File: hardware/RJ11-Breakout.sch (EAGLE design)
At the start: 8 parts

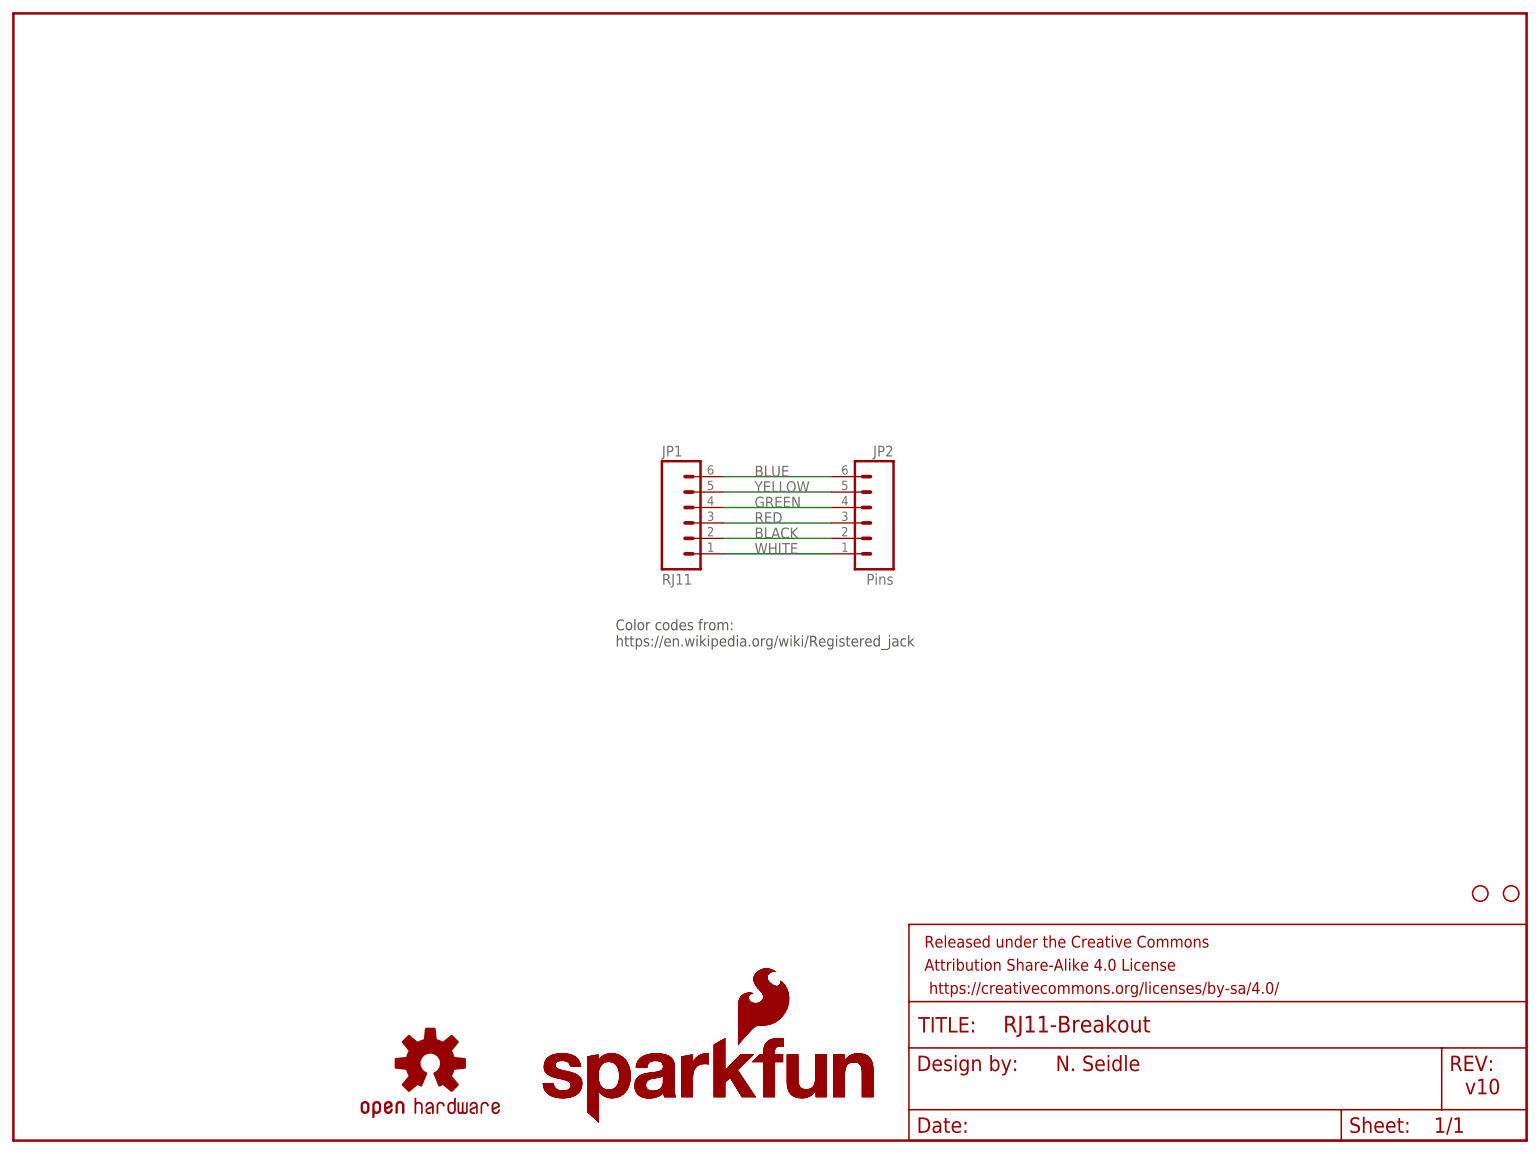
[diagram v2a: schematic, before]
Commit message: Creating panel of two
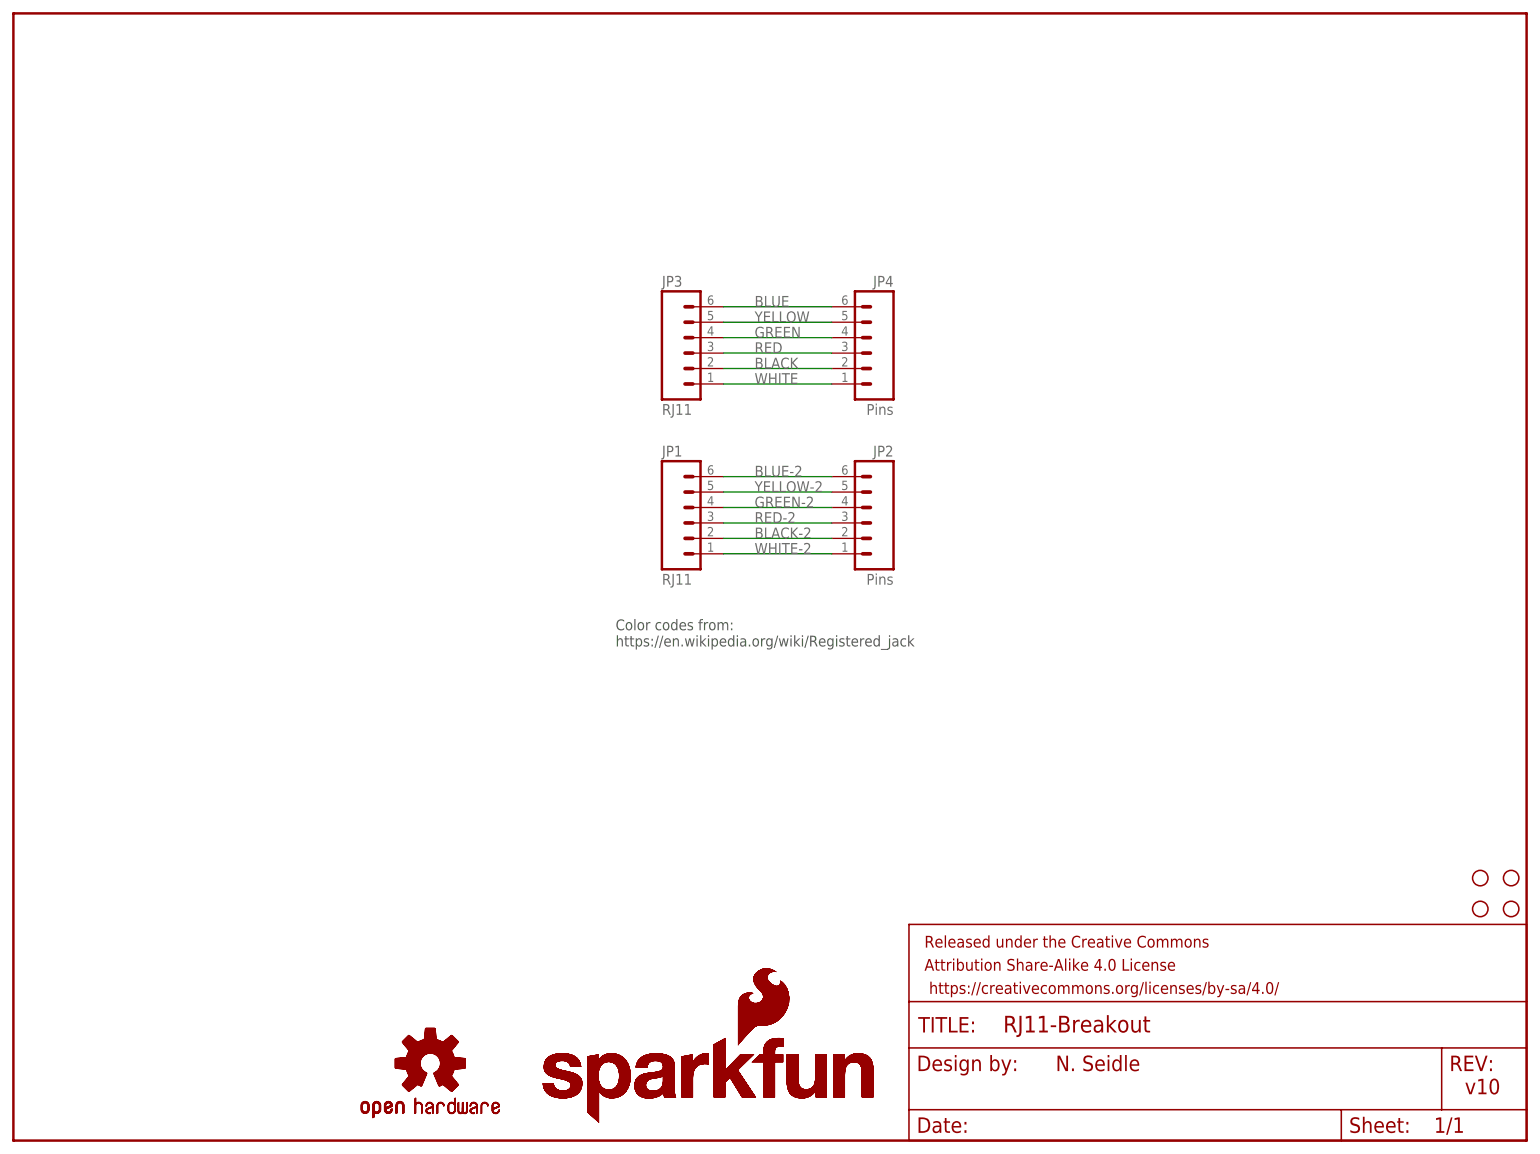
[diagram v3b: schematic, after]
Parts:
- added H2, H4: STAND-OFF, SparkFun-Electromechanical:STAND-OFF
- added JP3: RJ11, SparkFun-Connectors:RJ11-6PTH
- added JP4: Pins, SparkFun-Connectors:M06SILK_FEMALE_PTH
- added LOGO4, LOGO5: SFE_LOGO_NAME_FLAME.1_INCH, SparkFun-Aesthetics:SFE_LOGO_NAME_FLAME.1_INCH
- added LOGO6: OSHW-LOGOMINI, SparkFun-Aesthetics:OSHW-LOGOMINI
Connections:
- new net BLACK-2: JP1.2, JP2.2
- new net BLUE-2: JP1.6, JP2.6
- new net GREEN-2: JP1.4, JP2.4
- new net RED-2: JP1.3, JP2.3
- new net WHITE-2: JP1.1, JP2.1
- new net YELLOW-2: JP1.5, JP2.5
- net BLACK: now also JP3.2, JP4.2; no longer JP1.2, JP2.2
- net BLUE: now also JP3.6, JP4.6; no longer JP1.6, JP2.6
- net GREEN: now also JP3.4, JP4.4; no longer JP1.4, JP2.4
- net RED: now also JP3.3, JP4.3; no longer JP1.3, JP2.3
- net WHITE: now also JP3.1, JP4.1; no longer JP1.1, JP2.1
- net YELLOW: now also JP3.5, JP4.5; no longer JP1.5, JP2.5
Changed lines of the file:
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@@
 <part name="H1" library="SparkFun-Electromechanical" deviceset="STAND-OFF" device=""/>
 <part name="H3" library="SparkFun-Electromechanical" deviceset="STAND-OFF" device=""/>
+<part name="JP3" library="SparkFun-Connectors" deviceset="RJ11-6" device="PTH" value="RJ11"/>
+<part name="JP4" library="SparkFun-Connectors" deviceset="M06" device="SILK_FEMALE_PTH" value="Pins"/>
+<part name="H2" library="SparkFun-Electromechanical" deviceset="STAND-OFF" device=""/>
+<part name="H4" library="SparkFun-Electromechanical" deviceset="STAND-OFF" device=""/>
+<part name="LOGO4" library="SparkFun-Aesthetics" deviceset="SFE_LOGO_NAME_FLAME" device=".1_INCH"/>
+<part name="LOGO5" library="SparkFun-Aesthetics" deviceset="SFE_LOGO_NAME_FLAME" device=".1_INCH"/>
+<part name="LOGO6" library="SparkFun-Aesthetics" deviceset="OSHW-LOGO" device="MINI"/>
 </parts>
 <sheets>
@@
 <instance part="LOGO2" gate="G$1" x="86.36" y="2.54"/>
 <instance part="LOGO3" gate="G$1" x="68.58" y="12.7"/>
-<instance part="H1" gate="G$1" x="246.38" y="40.64"/>
-<instance part="H3" gate="G$1" x="241.3" y="40.64"/>
+<instance part="H1" gate="G$1" x="246.38" y="43.18"/>
+<instance part="H3" gate="G$1" x="241.3" y="43.18"/>
+<instance part="JP3" gate="G$1" x="111.76" y="129.54"/>
+<instance part="JP4" gate="G$1" x="139.7" y="129.54" rot="MR0"/>
+<instance part="H2" gate="G$1" x="241.3" y="38.1"/>
+<instance part="H4" gate="G$1" x="246.38" y="38.1"/>
+<instance part="LOGO4" gate="G$1" x="86.36" y="2.54"/>
+<instance part="LOGO5" gate="G$1" x="86.36" y="2.54"/>
+<instance part="LOGO6" gate="G$1" x="68.58" y="12.7"/>
 </instances>
 <busses>
@@
 <nets>
 <net name="WHITE" class="0">
+<segment>
+<pinref part="JP3" gate="G$1" pin="1"/>
+<pinref part="JP4" gate="G$1" pin="1"/>
+<wire x1="134.62" y1="124.46" x2="116.84" y2="124.46" width="0.1524" layer="91"/>
+<label x="121.92" y="124.46" size="1.778" layer="95"/>
+</segment>
+</net>
+<net name="BLACK" class="0">
+<segment>
+<pinref part="JP3" gate="G$1" pin="2"/>
+<pinref part="JP4" gate="G$1" pin="2"/>
+<wire x1="134.62" y1="127" x2="116.84" y2="127" width="0.1524" layer="91"/>
+<label x="121.92" y="127" size="1.778" layer="95"/>
+</segment>
+</net>
+<net name="RED" class="0">
+<segment>
+<pinref part="JP3" gate="G$1" pin="3"/>
+<pinref part="JP4" gate="G$1" pin="3"/>
+<wire x1="134.62" y1="129.54" x2="116.84" y2="129.54" width="0.1524" layer="91"/>
+<label x="121.92" y="129.54" size="1.778" layer="95"/>
+</segment>
+</net>
+<net name="GREEN" class="0">
+<segment>
+<pinref part="JP3" gate="G$1" pin="4"/>
+<pinref part="JP4" gate="G$1" pin="4"/>
+<wire x1="134.62" y1="132.08" x2="116.84" y2="132.08" width="0.1524" layer="91"/>
+<label x="121.92" y="132.08" size="1.778" layer="95"/>
+</segment>
+</net>
+<net name="YELLOW" class="0">
+<segment>
+<pinref part="JP3" gate="G$1" pin="5"/>
+<pinref part="JP4" gate="G$1" pin="5"/>
+<wire x1="134.62" y1="134.62" x2="116.84" y2="134.62" width="0.1524" layer="91"/>
+<label x="121.92" y="134.62" size="1.778" layer="95"/>
+</segment>
+</net>
+<net name="BLUE" class="0">
+<segment>
+<pinref part="JP3" gate="G$1" pin="6"/>
+<pinref part="JP4" gate="G$1" pin="6"/>
+<wire x1="134.62" y1="137.16" x2="116.84" y2="137.16" width="0.1524" layer="91"/>
+<label x="121.92" y="137.16" size="1.778" layer="95"/>
+</segment>
+</net>
+<net name="BLUE-2" class="0">
+<segment>
+<pinref part="JP1" gate="G$1" pin="6"/>
+<pinref part="JP2" gate="G$1" pin="6"/>
+<wire x1="134.62" y1="109.22" x2="116.84" y2="109.22" width="0.1524" layer="91"/>
+<label x="121.92" y="109.22" size="1.778" layer="95"/>
+</segment>
+</net>
+<net name="YELLOW-2" class="0">
+<segment>
+<pinref part="JP1" gate="G$1" pin="5"/>
+<pinref part="JP2" gate="G$1" pin="5"/>
+<wire x1="134.62" y1="106.68" x2="116.84" y2="106.68" width="0.1524" layer="91"/>
+<label x="121.92" y="106.68" size="1.778" layer="95"/>
+</segment>
+</net>
+<net name="GREEN-2" class="0">
+<segment>
+<pinref part="JP1" gate="G$1" pin="4"/>
+<pinref part="JP2" gate="G$1" pin="4"/>
+<wire x1="134.62" y1="104.14" x2="116.84" y2="104.14" width="0.1524" layer="91"/>
+<label x="121.92" y="104.14" size="1.778" layer="95"/>
+</segment>
+</net>
+<net name="RED-2" class="0">
+<segment>
+<pinref part="JP1" gate="G$1" pin="3"/>
+<pinref part="JP2" gate="G$1" pin="3"/>
+<wire x1="134.62" y1="101.6" x2="116.84" y2="101.6" width="0.1524" layer="91"/>
+<label x="121.92" y="101.6" size="1.778" layer="95"/>
+</segment>
+</net>
+<net name="BLACK-2" class="0">
+<segment>
+<pinref part="JP1" gate="G$1" pin="2"/>
+<pinref part="JP2" gate="G$1" pin="2"/>
+<wire x1="134.62" y1="99.06" x2="116.84" y2="99.06" width="0.1524" layer="91"/>
+<label x="121.92" y="99.06" size="1.778" layer="95"/>
+</segment>
+</net>
+<net name="WHITE-2" class="0">
 <segment>
 <pinref part="JP1" gate="G$1" pin="1"/>
@@
 </segment>
 </net>
-<net name="BLACK" class="0">
-<segment>
-<pinref part="JP1" gate="G$1" pin="2"/>
-<pinref part="JP2" gate="G$1" pin="2"/>
-<wire x1="134.62" y1="99.06" x2="116.84" y2="99.06" width="0.1524" layer="91"/>
-<label x="121.92" y="99.06" size="1.778" layer="95"/>
-</segment>
-</net>
-<net name="RED" class="0">
-<segment>
-<pinref part="JP1" gate="G$1" pin="3"/>
-<pinref part="JP2" gate="G$1" pin="3"/>
-<wire x1="134.62" y1="101.6" x2="116.84" y2="101.6" width="0.1524" layer="91"/>
-<label x="121.92" y="101.6" size="1.778" layer="95"/>
-</segment>
-</net>
-<net name="GREEN" class="0">
-<segment>
-<pinref part="JP1" gate="G$1" pin="4"/>
-<pinref part="JP2" gate="G$1" pin="4"/>
-<wire x1="134.62" y1="104.14" x2="116.84" y2="104.14" width="0.1524" layer="91"/>
-<label x="121.92" y="104.14" size="1.778" layer="95"/>
-</segment>
-</net>
-<net name="YELLOW" class="0">
-<segment>
-<pinref part="JP1" gate="G$1" pin="5"/>
-<pinref part="JP2" gate="G$1" pin="5"/>
-<wire x1="134.62" y1="106.68" x2="116.84" y2="106.68" width="0.1524" layer="91"/>
-<label x="121.92" y="106.68" size="1.778" layer="95"/>
-</segment>
-</net>
-<net name="BLUE" class="0">
-<segment>
-<pinref part="JP1" gate="G$1" pin="6"/>
-<pinref part="JP2" gate="G$1" pin="6"/>
-<wire x1="134.62" y1="109.22" x2="116.84" y2="109.22" width="0.1524" layer="91"/>
-<label x="121.92" y="109.22" size="1.778" layer="95"/>
-</segment>
-</net>
